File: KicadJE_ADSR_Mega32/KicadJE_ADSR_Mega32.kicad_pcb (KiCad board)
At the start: 2 copper layers, 100 x 100 mm, 134 parts, among them J101 ADSR1, J102 ADSR2, J103 ADSR1, J104 ADSR2, J105 ADSR1-G8, J106 ADSR2-G8, J107 ADSR4-G8, J108 ADSR3-G8, J201 AVR-ISP-6, J202 UART, J301 In, J302 +5V reg/doepfer, J303 Out, J304 CV_time, J305 CV doepfer, P101 Doepfer_Power_16pin, P302 Doepfer_Power_16pin, Q301 BC337, Q302 PZT2222A, U201 ATmega32A-AU, U301 L78L05_TO92, U302 PT2399, Y201 16MHz

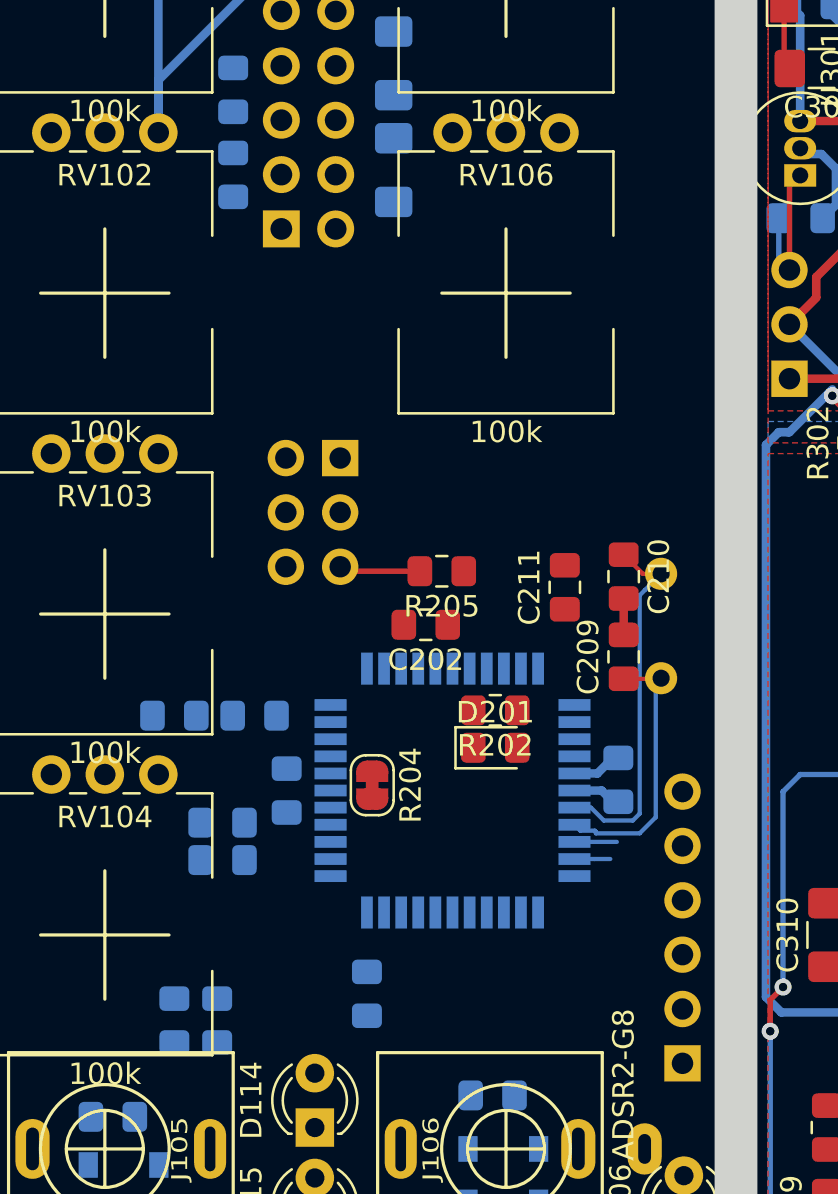
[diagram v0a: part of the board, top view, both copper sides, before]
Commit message: Update KicadJE_ADSR_Mega32.kicad_pcb
Power rerouted to Atmega32
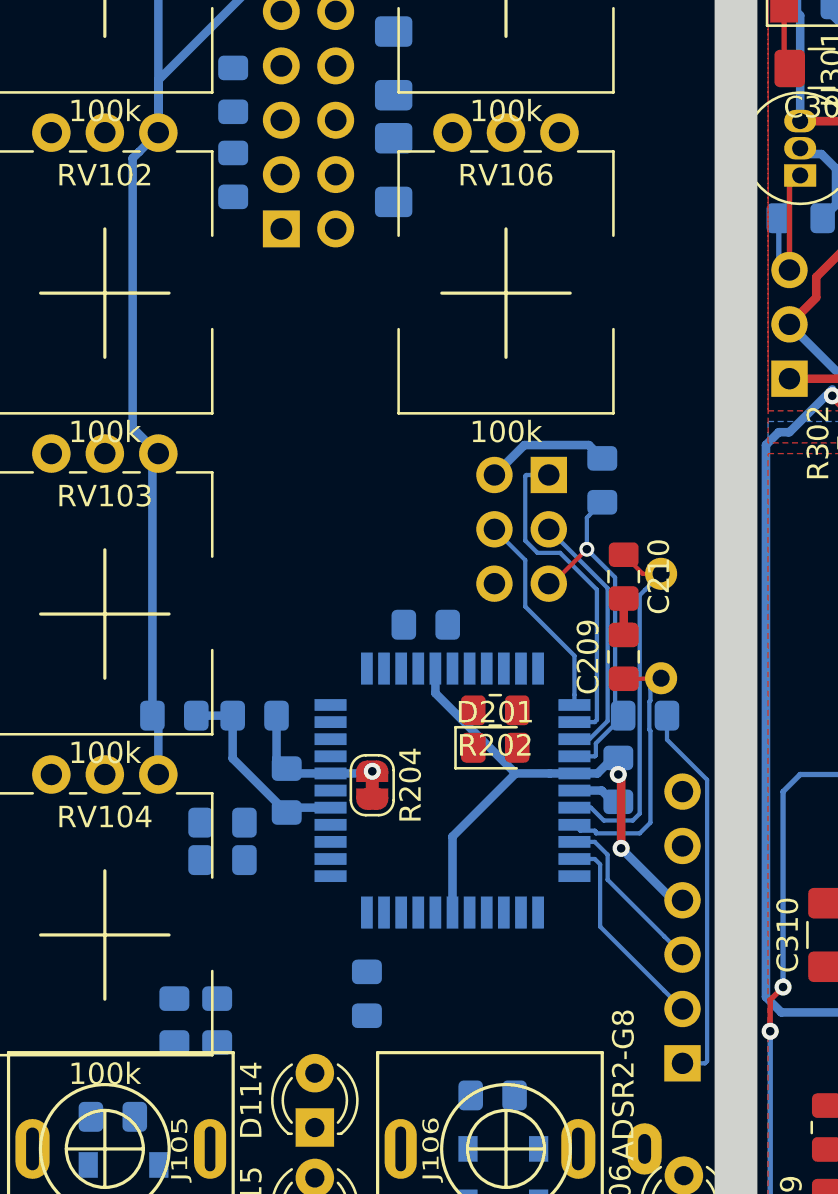
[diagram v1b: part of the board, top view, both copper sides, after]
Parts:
- C202, C211, R205: moved to B.Cu
- moved J201 9.78 mm to (80.8, 83.5)
- moved R205 8.62 mm to (83.2, 83.8), turned to 270 degrees
- moved C211 7.08 mm to (85.2, 94.8), turned to 0 degrees
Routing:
- net +5V: track 58.5 -> 120.2 mm, vias 1 -> 3
- net Net-(C211-Pad2): track 0.00 -> 18.1 mm
- net 6_MISO: track 0.00 -> 15.6 mm
- net reset: track 3.81 -> 16.5 mm, vias 0 -> 1
- net 7_SCK: track 0.00 -> 12.0 mm
- net 5_MOSI: track 0.00 -> 9.76 mm
- net +5VA: track 41.9 -> 51.3 mm
- net 9_Tx: track 1.67 -> 9.66 mm
- net GNDA: track 26.9 -> 33.7 mm, vias 3 -> 4
- net 8_Rx: track 1.98 -> 7.92 mm

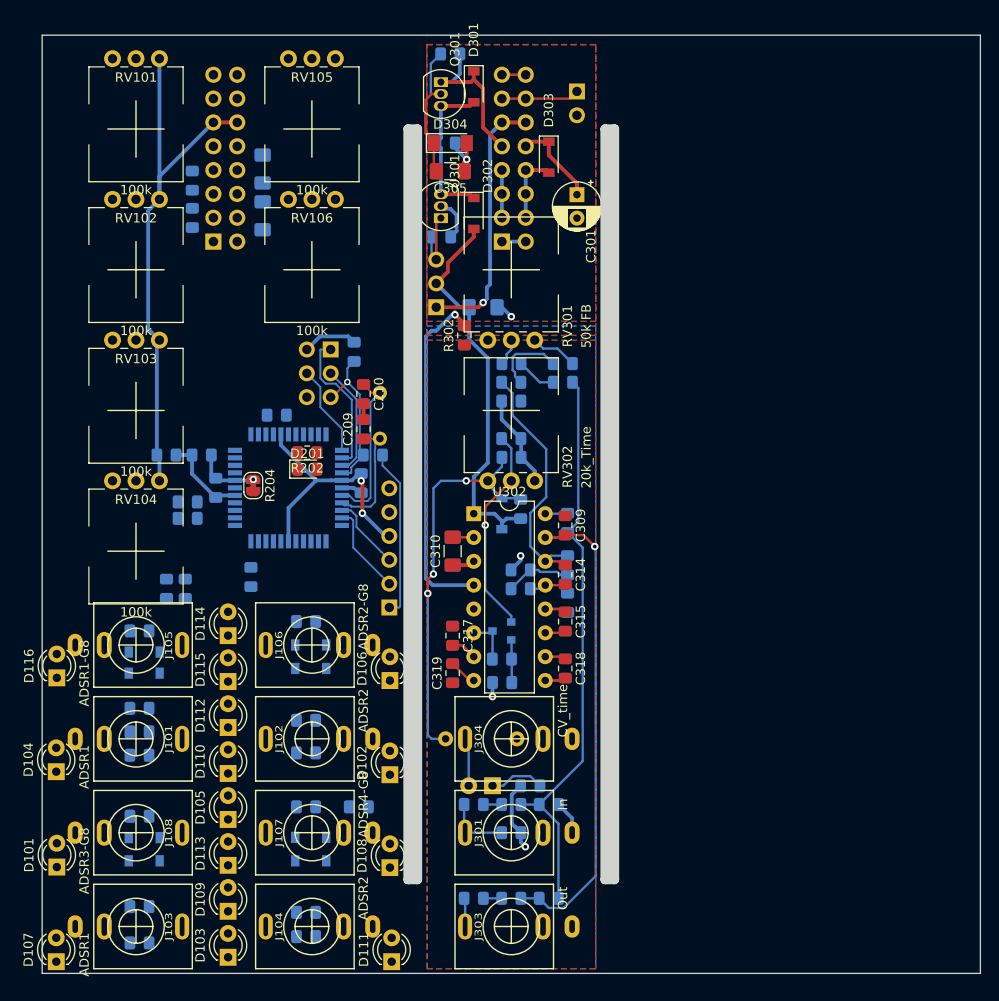
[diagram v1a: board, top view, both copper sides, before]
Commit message: Update KicadJE_ADSR_Mega32.kicad_pcb
GND fill
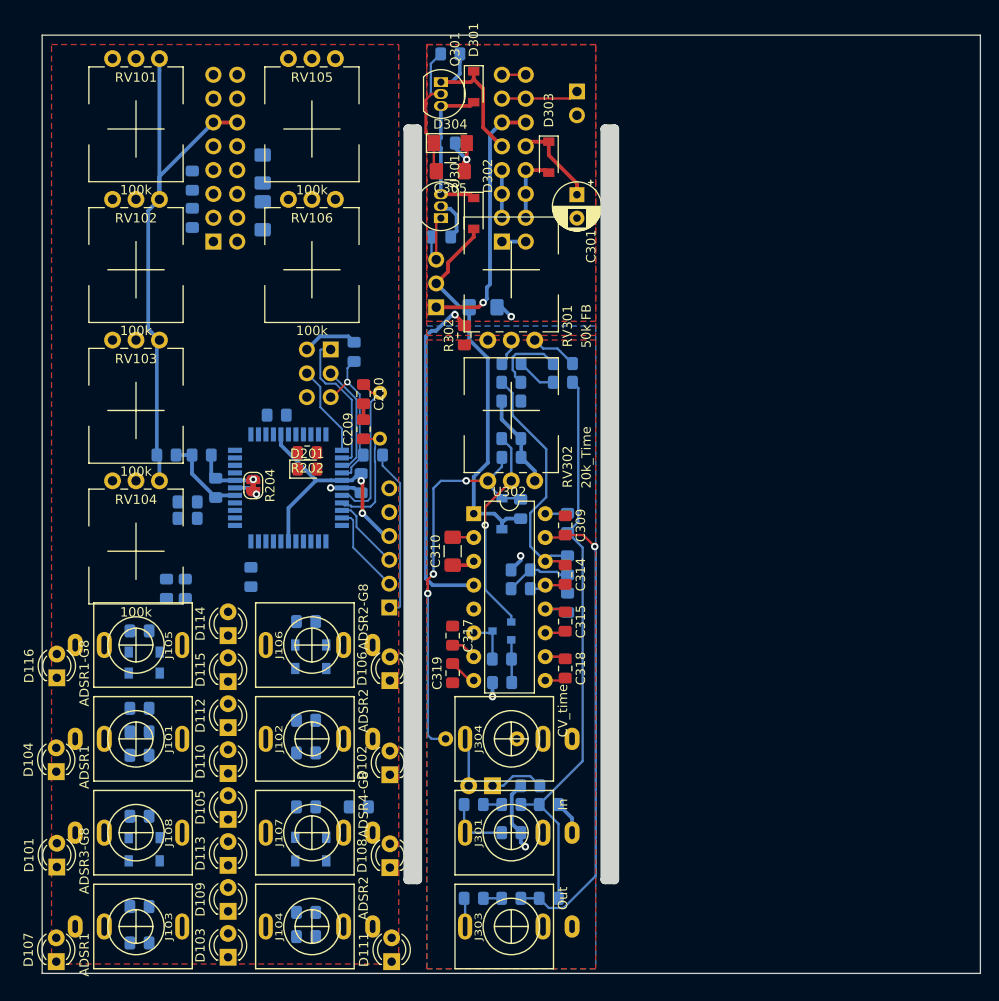
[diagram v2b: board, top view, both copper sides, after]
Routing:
- net GND: track 65.4 -> 69.1 mm, vias 3 -> 5
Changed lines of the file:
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@@
     (thickness 1.6)
     (drawings 27)
-    (tracks 365)
+    (tracks 370)
     (zones 0)
     (modules 134)
@@
   (segment (start 81.95 98.25) (end 83.225 98.25) (width 0.4) (layer B.Cu) (net 2))
   (segment (start 84.25 90.975) (end 84.25 89.275) (width 0.4) (layer F.Cu) (net 2))
+  (via (at 72.831841 98.930377) (size 0.8) (drill 0.4) (layers F.Cu B.Cu) (net 2))
+  (segment (start 70.55 98.25) (end 72.151464 98.25) (width 0.4) (layer B.Cu) (net 2))
+  (segment (start 72.151464 98.25) (end 72.831841 98.930377) (width 0.4) (layer B.Cu) (net 2))
+  (via (at 80.75 98.25) (size 0.8) (drill 0.4) (layers F.Cu B.Cu) (net 2))
+  (segment (start 81.95 98.25) (end 80.75 98.25) (width 0.4) (layer B.Cu) (net 2))
   (segment (start 98.2 101) (end 99 101.8) (width 0.4) (layer B.Cu) (net 3))
   (segment (start 96 101) (end 98.2 101) (width 0.4) (layer B.Cu) (net 3))
@@
       )
     )
+  )
+  (zone (net 2) (net_name GND) (layer F.Cu) (hatch edge 0.508)
+    (connect_pads (clearance 0.508))
+    (min_thickness 0.254)
+    (fill yes (arc_segments 32) (thermal_gap 0.508) (thermal_bridge_width 0.508))
+    (polygon
+      (pts
+        (xy 51 51) (xy 88 51) (xy 88 149) (xy 51 149)
+      )
+    )

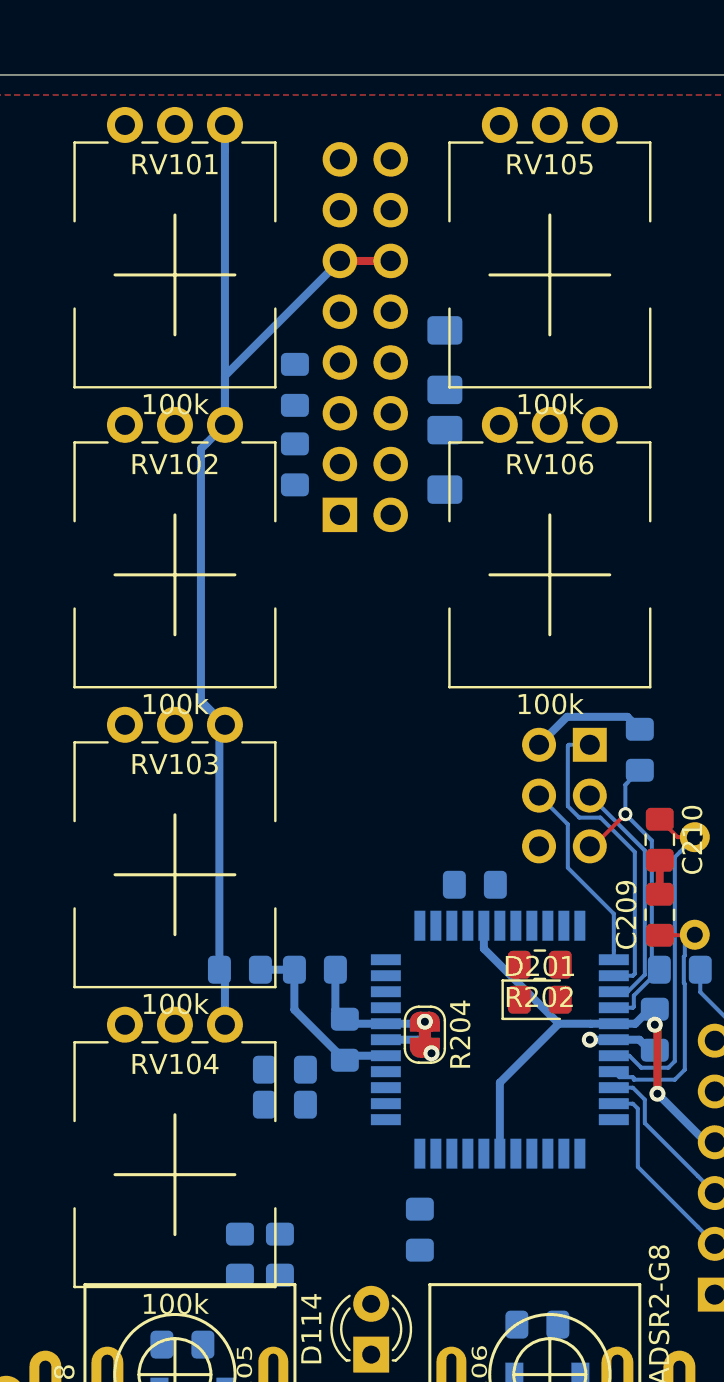
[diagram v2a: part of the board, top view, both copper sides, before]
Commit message: Update KicadJE_ADSR_Mega32.kicad_pcb
Top section routed initially
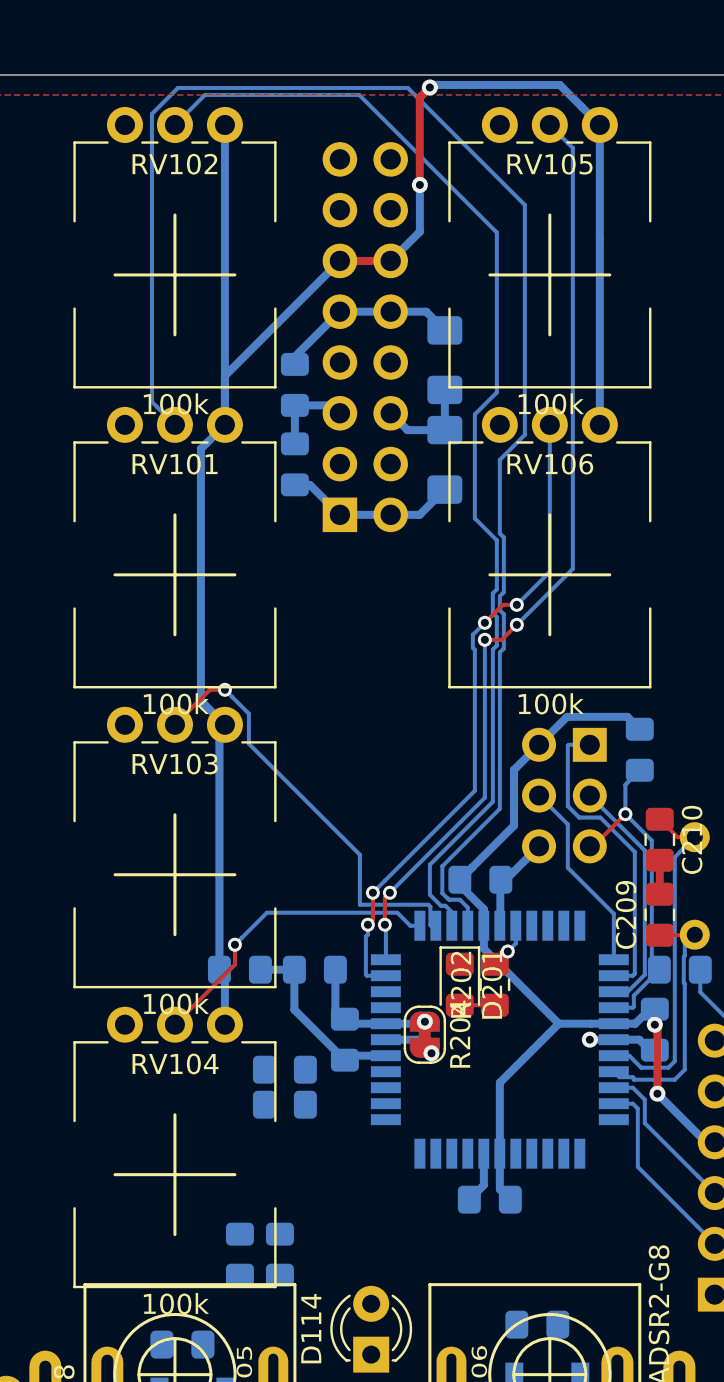
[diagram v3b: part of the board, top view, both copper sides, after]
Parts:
- moved RV101 15.0 mm to (57.5, 67.5)
- moved RV102 15.0 mm to (57.5, 52.5)
- moved D201 4.07 mm to (74.2, 95.5), turned to 270 degrees
- moved C203 3.81 mm to (75.8, 106.2), turned to 0 degrees
- moved R202 2.46 mm to (76.0, 95.5), turned to 90 degrees
- moved C202 0.37 mm to (75.3, 90.2)
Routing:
- net 24_A0: track 0.00 -> 76.6 mm
- net 25_A1: track 0.00 -> 57.3 mm
- net +5V: track 120.2 -> 167.6 mm, vias 3 -> 5
- net 28_A4: track 0.00 -> 46.6 mm, vias 0 -> 4
- net 29_A5: track 0.00 -> 32.8 mm, vias 0 -> 4
- net 26_A2: track 0.00 -> 21.5 mm, vias 0 -> 1
- net GND: track 69.1 -> 85.9 mm
- net 27_A3: track 0.00 -> 15.4 mm, vias 0 -> 1
- net +12V: track 0.00 -> 9.20 mm
- net -12V: track 0.00 -> 8.64 mm
- net 0_LED: track 0.00 -> 2.36 mm, vias 0 -> 1
- net Net-(D201-Pad2): track 0.00 -> 1.75 mm

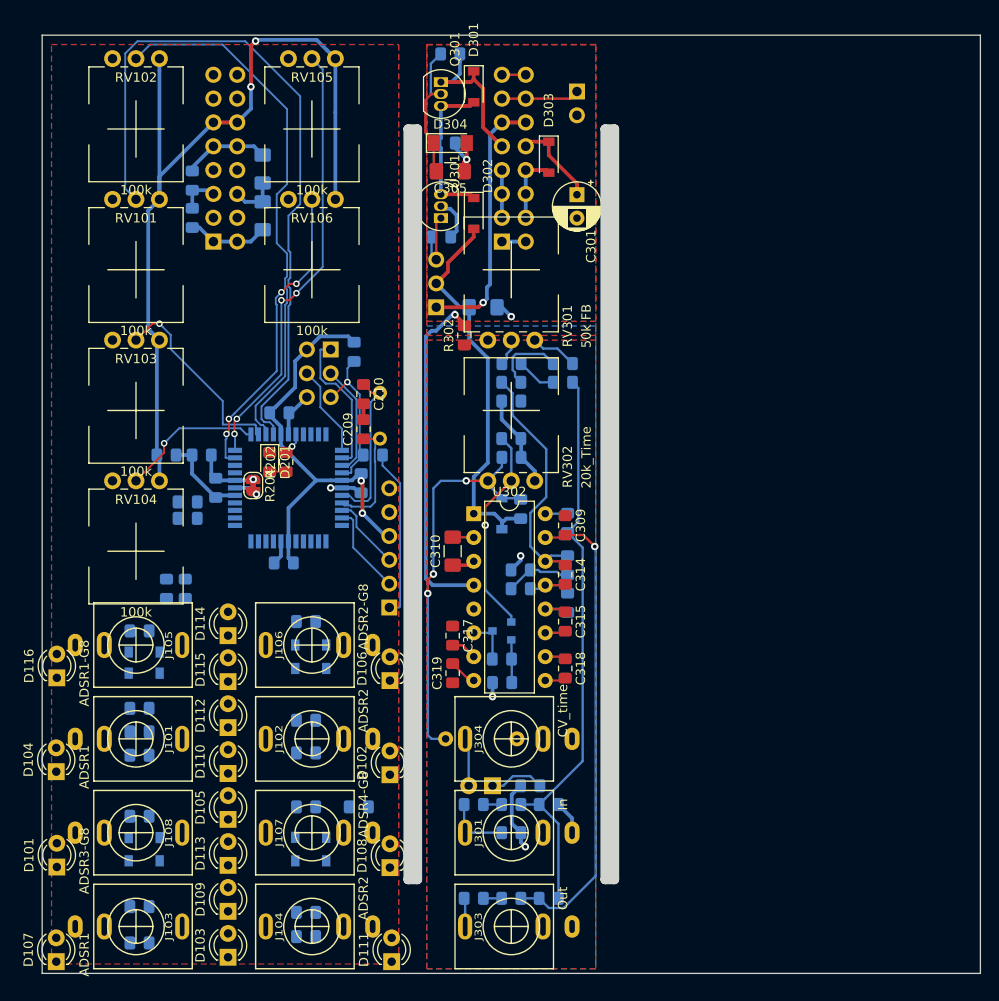
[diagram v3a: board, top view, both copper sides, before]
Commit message: GNDA for all IO
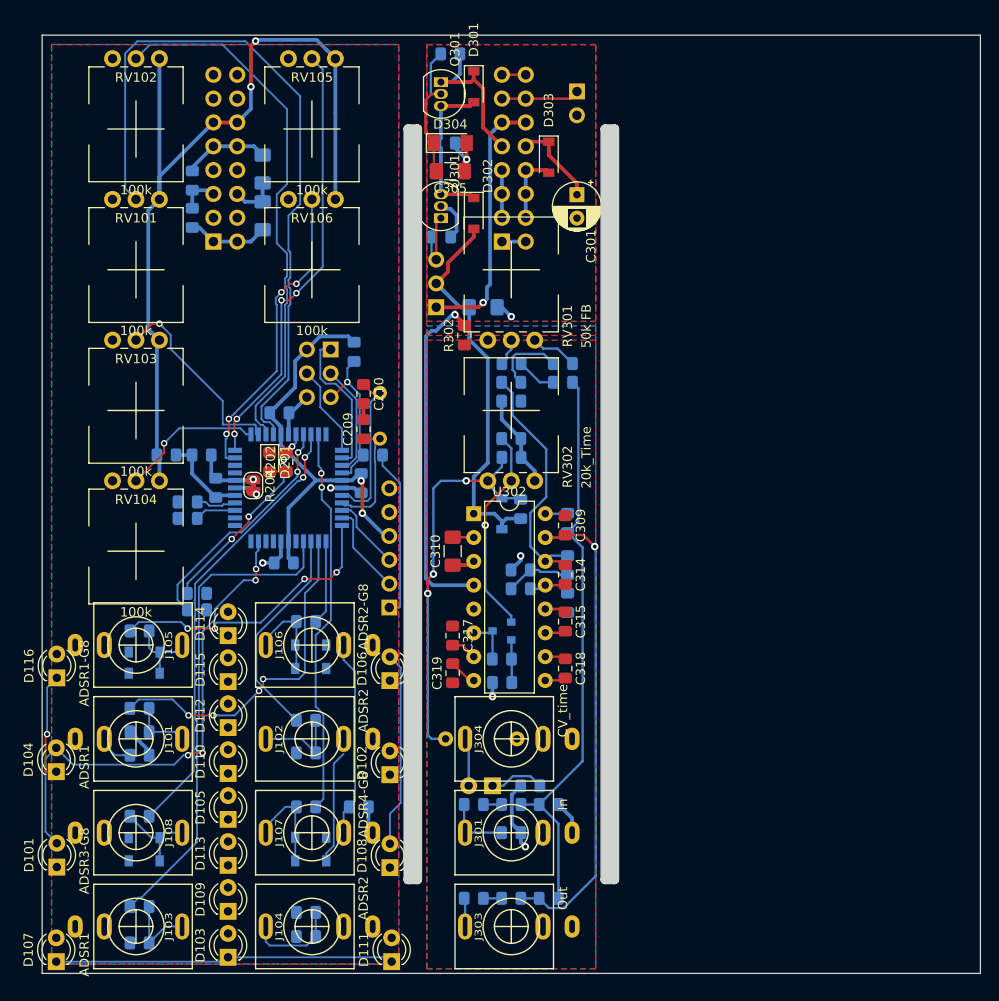
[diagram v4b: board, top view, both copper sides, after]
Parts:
- moved R103 3.95 mm to (66.5, 111.2), turned to 0 degrees
- moved R104 1.35 mm to (66.5, 109.5), turned to 0 degrees
- turned D119 to 180 degrees
- turned D120 to 0 degrees
- turned D123 to 180 degrees
- turned D124 to 0 degrees
- turned R105 to 0 degrees
- turned R110 to 0 degrees
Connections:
- D118 pad 2: GND -> GNDA
- D120 pad 2: GND -> GNDA
- D122 pad 2: GND -> GNDA
- D123 pad 1: (no net) -> +5V
- D124 pad 2: GND -> GNDA
- J105 pad TN: GNDA -> Net-(J105-PadTN)
- J106 pad TN: GNDA -> Net-(J105-PadTN)
- J107 pad TN: Net-(J107-PadTN) -> Net-(J105-PadTN)
- J108 pad TN: GNDA -> Net-(J105-PadTN)
- R110 pad 1: GNDA -> Net-(J105-PadTN)
- R110 pad 2: Net-(J107-PadTN) -> GNDA
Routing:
- net 18: track 0.00 -> 53.8 mm, vias 0 -> 4
- net 14_PWM: track 0.00 -> 52.0 mm
- net 2_INT2: track 0.00 -> 48.0 mm, vias 0 -> 2
- net 3_PWM: track 0.00 -> 41.6 mm, vias 0 -> 2
- net 12_PWM: track 0.00 -> 36.7 mm, vias 0 -> 4
- net Net-(D103-Pad1): track 0.00 -> 36.1 mm
- net 10_INT0: track 0.00 -> 30.7 mm, vias 0 -> 4
- net 1: track 0.00 -> 25.4 mm, vias 0 -> 2
- net 13_PWM: track 0.00 -> 23.3 mm
- net Net-(J105-PadTN): track 0.00 -> 21.0 mm
- net 19: track 0.00 -> 20.9 mm
- net 0_LED: track 2.36 -> 21.7 mm, vias 1 -> 4
- net +5V: track 167.6 -> 179.7 mm
- net Net-(D104-Pad1): track 0.00 -> 11.6 mm, vias 0 -> 1
- net ADSR4-G8: track 0.00 -> 10.7 mm
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- added copper zone on B.Cu, net +5V

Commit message: Update KicadJE_ADSR_Mega32.kicad_pcb
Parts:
- moved D119 1.14 mm to (77.5, 117.3)
- moved D120 1.13 mm to (77.5, 115.0)
- moved R112 0.46 mm to (77.7, 123.2)
- moved C102 0.43 mm to (77.7, 126.5)
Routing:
- net Net-(D101-Pad1): track 0.00 -> 88.5 mm
- net 19: track 20.9 -> 101.9 mm, vias 0 -> 8
- net Net-(D102-Pad1): track 0.00 -> 73.4 mm, vias 0 -> 5
- net 18: track 53.8 -> 125.6 mm, vias 4 -> 8
- net Net-(D104-Pad1): track 11.6 -> 82.6 mm, vias 1 -> 7
- net 20: track 0.00 -> 50.3 mm, vias 0 -> 2
- net 15_PWM: track 0.00 -> 50.0 mm, vias 0 -> 2
- net 21: track 0.00 -> 41.9 mm, vias 0 -> 2
- net GNDA: track 40.1 -> 66.4 mm, vias 4 -> 12
- net Net-(J105-PadTN): track 21.0 -> 44.5 mm, vias 0 -> 2
- net ADSR2-G8: track 9.74 -> 4.69 mm
- net +5V: track 179.7 -> 175.1 mm, vias 5 -> 6
- net 10_INT0: track 30.7 -> 31.8 mm
- net 3_PWM: track 41.6 -> 42.4 mm
